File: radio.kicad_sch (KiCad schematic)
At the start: 28 parts, among them IC4 S2-LPQTR, IC5 BALF-SPI2-01D3, Y3 Crystal_GND24

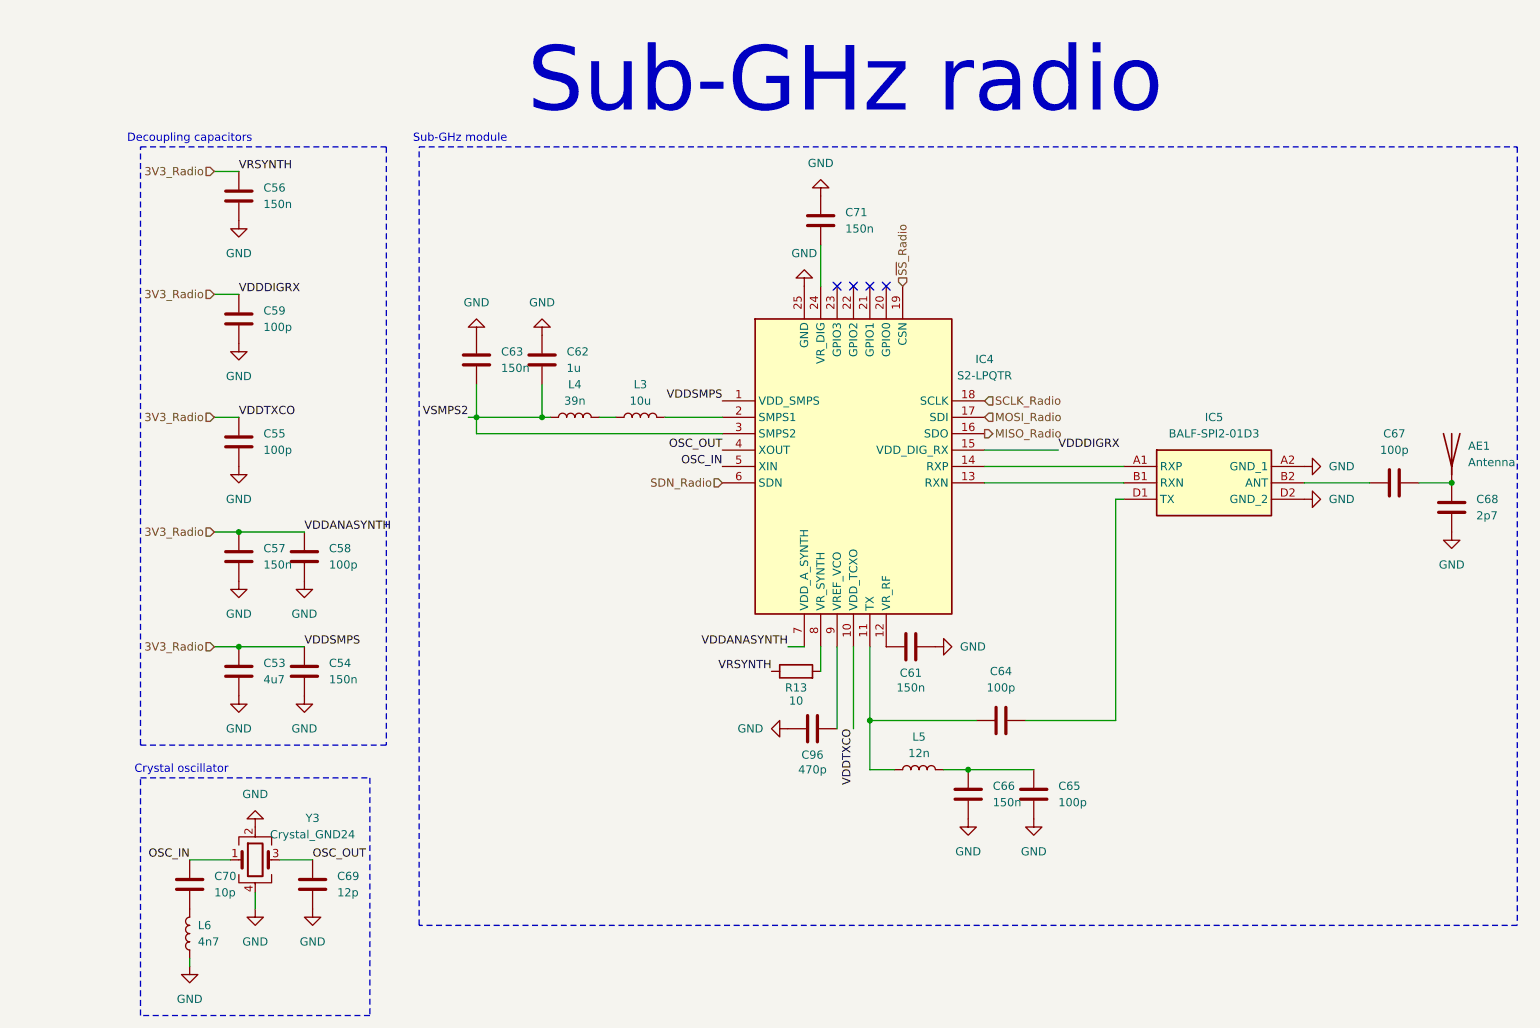
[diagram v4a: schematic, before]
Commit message: Fix some little warnings and refomat schematics files
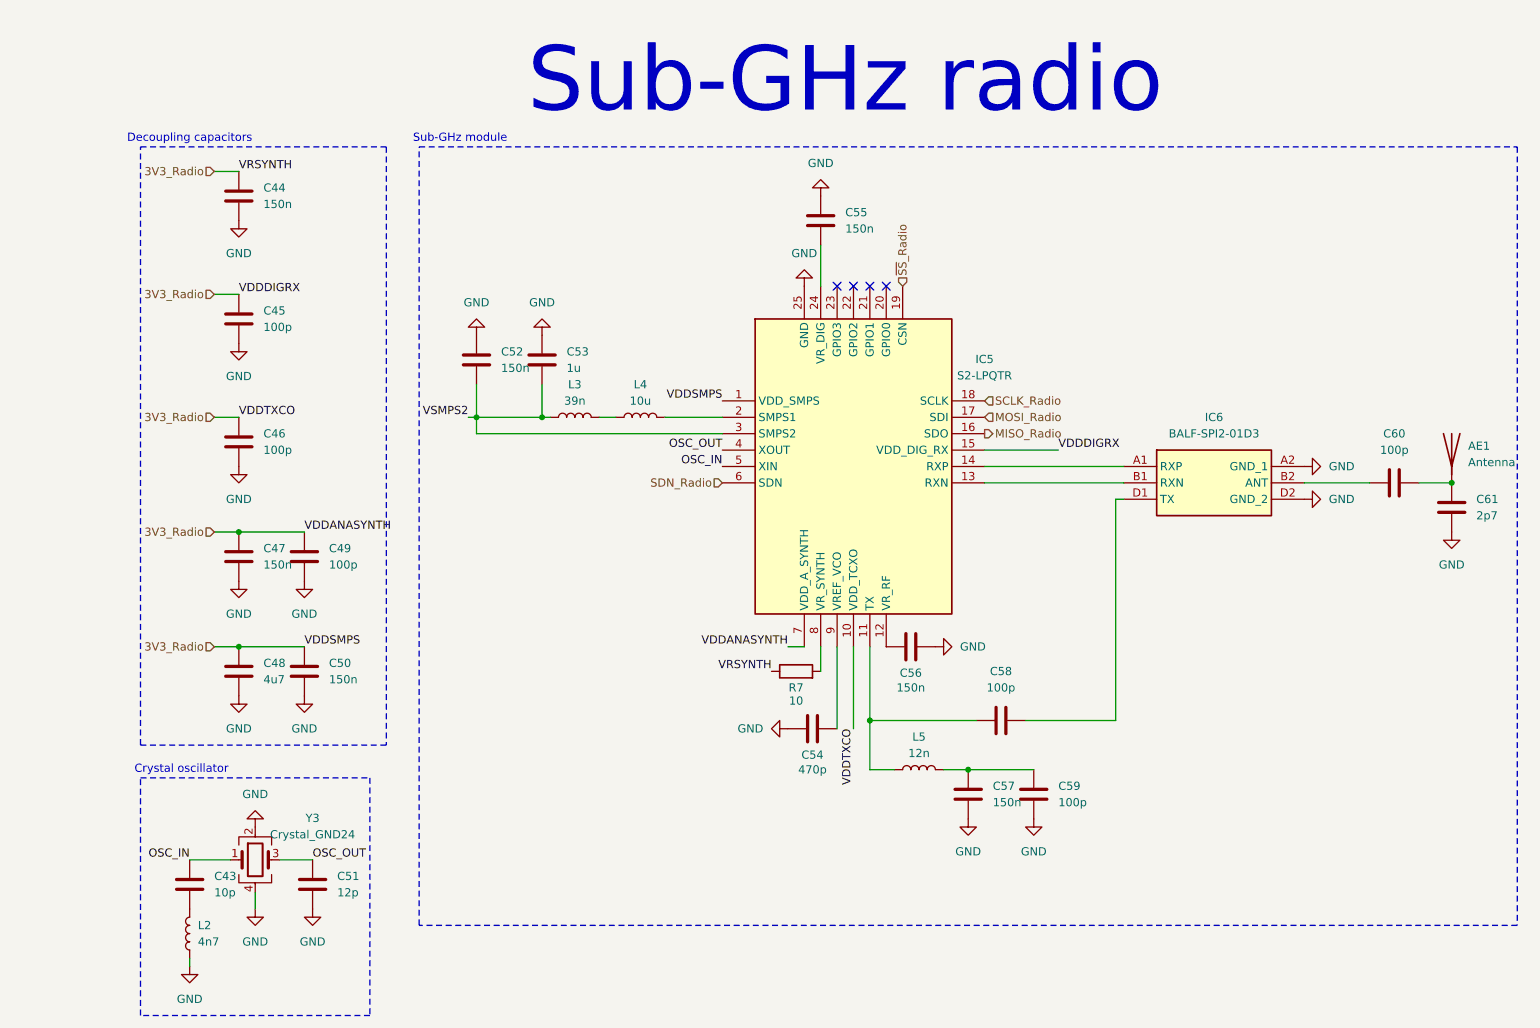
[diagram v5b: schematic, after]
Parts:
- renumbered C70 to C43, C56 to C44, C59 to C45, C55 to C46, C57 to C47, C53 to C48, C58 to C49, C54 to C50, C69 to C51, C63 to C52, C62 to C53, C96 to C54, C71 to C55, C61 to C56, C66 to C57, C64 to C58, C65 to C59, C67 to C60, C68 to C61, IC4 to IC5, IC5 to IC6, L6 to L2, L4 to L3, L3 to L4, R13 to R7

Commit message: Assign 0603 footprint to all capacitors
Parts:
- C43, C44, C45, C46, C47, C48, C49, C50, C51, C52, C53, C54, C55, C56, C57, C58, C59, C60, C61: footprint (none) -> Capacitor_SMD:C_0603_1608Metric_Pad1.08x0.95mm_HandSolder
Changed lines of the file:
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@@
 			)
 		)
-		(property "Footprint" ""
+		(property "Footprint" "Capacitor_SMD:C_0603_1608Metric_Pad1.08x0.95mm_HandSolder"
 			(at 55.5752 120.65 0)
 			(effects
@@
 			)
 		)
-		(property "Footprint" ""
+		(property "Footprint" "Capacitor_SMD:C_0603_1608Metric_Pad1.08x0.95mm_HandSolder"
 			(at 143.8148 43.18 0)
 			(effects
@@
 			)
 		)
-		(property "Footprint" ""
+		(property "Footprint" "Capacitor_SMD:C_0603_1608Metric_Pad1.08x0.95mm_HandSolder"
 			(at 55.5752 46.99 0)
 			(effects
@@
 			)
 		)
-		(property "Footprint" ""
+		(property "Footprint" "Capacitor_SMD:C_0603_1608Metric_Pad1.08x0.95mm_HandSolder"
 			(at 176.53 123.4948 0)
 			(effects
@@
 			)
 		)
-		(property "Footprint" ""
+		(property "Footprint" "Capacitor_SMD:C_0603_1608Metric_Pad1.08x0.95mm_HandSolder"
 			(at 229.87 88.5952 0)
 			(effects
@@
 			)
 		)
-		(property "Footprint" ""
+		(property "Footprint" "Capacitor_SMD:C_0603_1608Metric_Pad1.08x0.95mm_HandSolder"
 			(at 55.5752 85.09 0)
 			(effects
@@
 			)
 		)
-		(property "Footprint" ""
+		(property "Footprint" "Capacitor_SMD:C_0603_1608Metric_Pad1.08x0.95mm_HandSolder"
 			(at 90.4748 64.77 0)
 			(effects
@@
 			)
 		)
-		(property "Footprint" ""
+		(property "Footprint" "Capacitor_SMD:C_0603_1608Metric_Pad1.08x0.95mm_HandSolder"
 			(at 65.7352 120.65 0)
 			(effects
@@
 			)
 		)
-		(property "Footprint" ""
+		(property "Footprint" "Capacitor_SMD:C_0603_1608Metric_Pad1.08x0.95mm_HandSolder"
 			(at 147.32 124.7648 0)
 			(effects
@@
 			)
 		)
-		(property "Footprint" ""
+		(property "Footprint" "Capacitor_SMD:C_0603_1608Metric_Pad1.08x0.95mm_HandSolder"
 			(at 241.6048 87.63 0)
 			(effects
@@
 			)
 		)
-		(property "Footprint" ""
+		(property "Footprint" "Capacitor_SMD:C_0603_1608Metric_Pad1.08x0.95mm_HandSolder"
 			(at 162.56 112.0648 0)
 			(effects
@@
 			)
 		)
-		(property "Footprint" ""
+		(property "Footprint" "Capacitor_SMD:C_0603_1608Metric_Pad1.08x0.95mm_HandSolder"
 			(at 168.6052 139.7 0)
 			(effects
@@
 			)
 		)
-		(property "Footprint" ""
+		(property "Footprint" "Capacitor_SMD:C_0603_1608Metric_Pad1.08x0.95mm_HandSolder"
 			(at 65.0748 146.05 0)
 			(effects
@@
 			)
 		)
-		(property "Footprint" ""
+		(property "Footprint" "Capacitor_SMD:C_0603_1608Metric_Pad1.08x0.95mm_HandSolder"
 			(at 100.6348 64.77 0)
 			(effects
@@
 			)
 		)
-		(property "Footprint" ""
+		(property "Footprint" "Capacitor_SMD:C_0603_1608Metric_Pad1.08x0.95mm_HandSolder"
 			(at 55.5752 102.87 0)
 			(effects
@@
 			)
 		)
-		(property "Footprint" ""
+		(property "Footprint" "Capacitor_SMD:C_0603_1608Metric_Pad1.08x0.95mm_HandSolder"
 			(at 65.7352 102.87 0)
 			(effects
@@
 			)
 		)
-		(property "Footprint" ""
+		(property "Footprint" "Capacitor_SMD:C_0603_1608Metric_Pad1.08x0.95mm_HandSolder"
 			(at 46.0248 146.05 0)
 			(effects
@@
 			)
 		)
-		(property "Footprint" ""
+		(property "Footprint" "Capacitor_SMD:C_0603_1608Metric_Pad1.08x0.95mm_HandSolder"
 			(at 176.8348 132.08 0)
 			(effects
@@
 			)
 		)
-		(property "Footprint" ""
+		(property "Footprint" "Capacitor_SMD:C_0603_1608Metric_Pad1.08x0.95mm_HandSolder"
 			(at 55.5752 66.04 0)
 			(effects

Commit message: Assign 0603 footprints to all resistors
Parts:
- R7: footprint (none) -> Resistor_SMD:R_0603_1608Metric_Pad0.98x0.95mm_HandSolder
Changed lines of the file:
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@@
 			)
 		)
-		(property "Footprint" ""
+		(property "Footprint" "Resistor_SMD:R_0603_1608Metric_Pad0.98x0.95mm_HandSolder"
 			(at 140.97 118.618 90)
 			(effects
